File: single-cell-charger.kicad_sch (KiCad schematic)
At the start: 12 parts

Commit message: Lots of cleanup and updates; Waiting on PR approval for GPS filter
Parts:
- renumbered C35 to C43, C36 to C44, C37 to C45, D17 to D19, D18 to D20, U10 to U13, U11 to U14

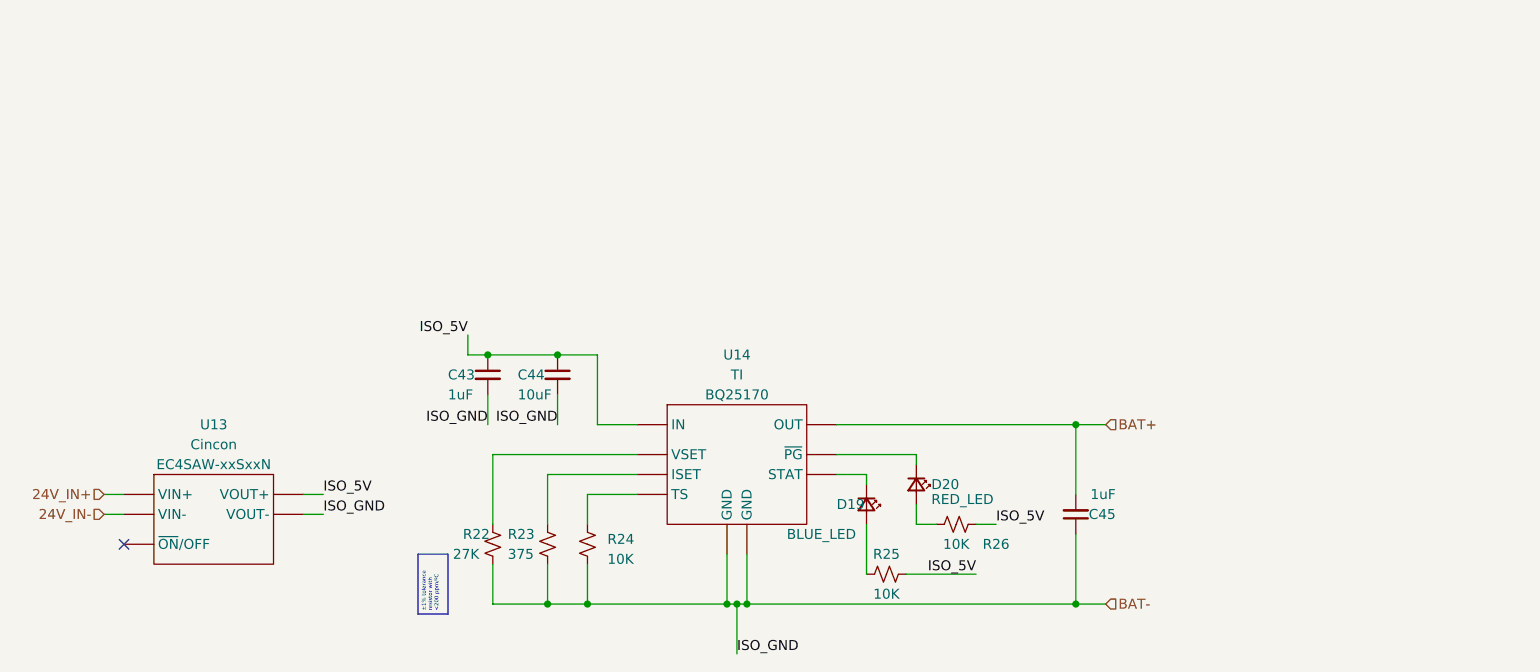
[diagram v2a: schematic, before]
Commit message: Added stat sense in REDs; kicad V8.01
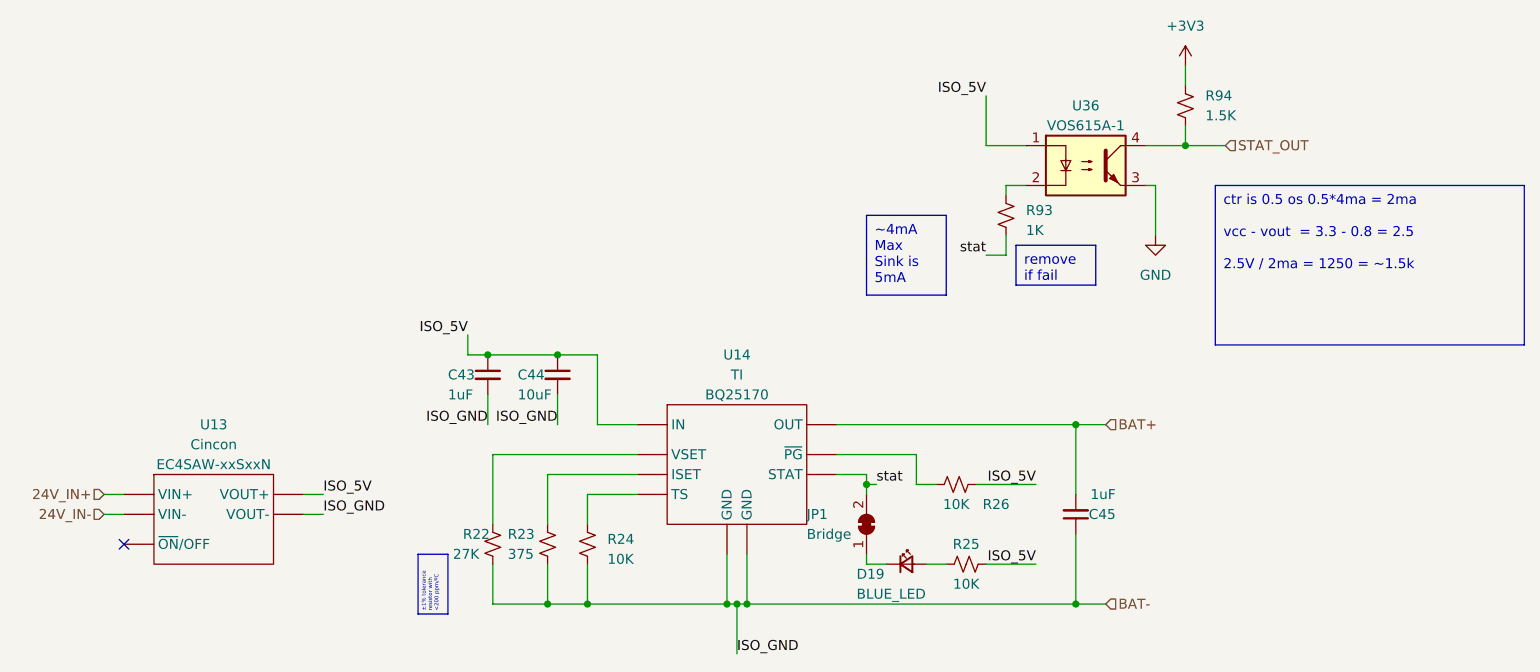
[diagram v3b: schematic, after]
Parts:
- removed D20: RED_LED, LED_SMD:LED_0603_1608Metric_Pad1.05x0.95mm_HandSolder, symbol Device:LED_Small
- added JP1: Bridge, symbol Jumper:SolderJumper_2_Bridged
- added R93: 1K, symbol Device:R_Small_US
- added R94: 1.5K, symbol Device:R_Small_US
- added U36: VOS615A-1, symbol Isolator:VO615A-1
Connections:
- net ISO_5V: now also U36.1
- net at R26.1: now also U14.6 (~{PG})
- net at D19.1 (K): now also JP1.1 (A); no longer U14.5 (STAT)
- new net: R93.1, U36.2
- new net +3V3: R94.1
- new net GND: U36.3
- new net STAT_OUT: R94.2, U36.4
- new net stat: JP1.2 (B), R93.2, U14.5 (STAT)
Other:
- moved on the sheet: D19, R25, R26

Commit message: 8.02 Update; Also changed VRMs and added some notes
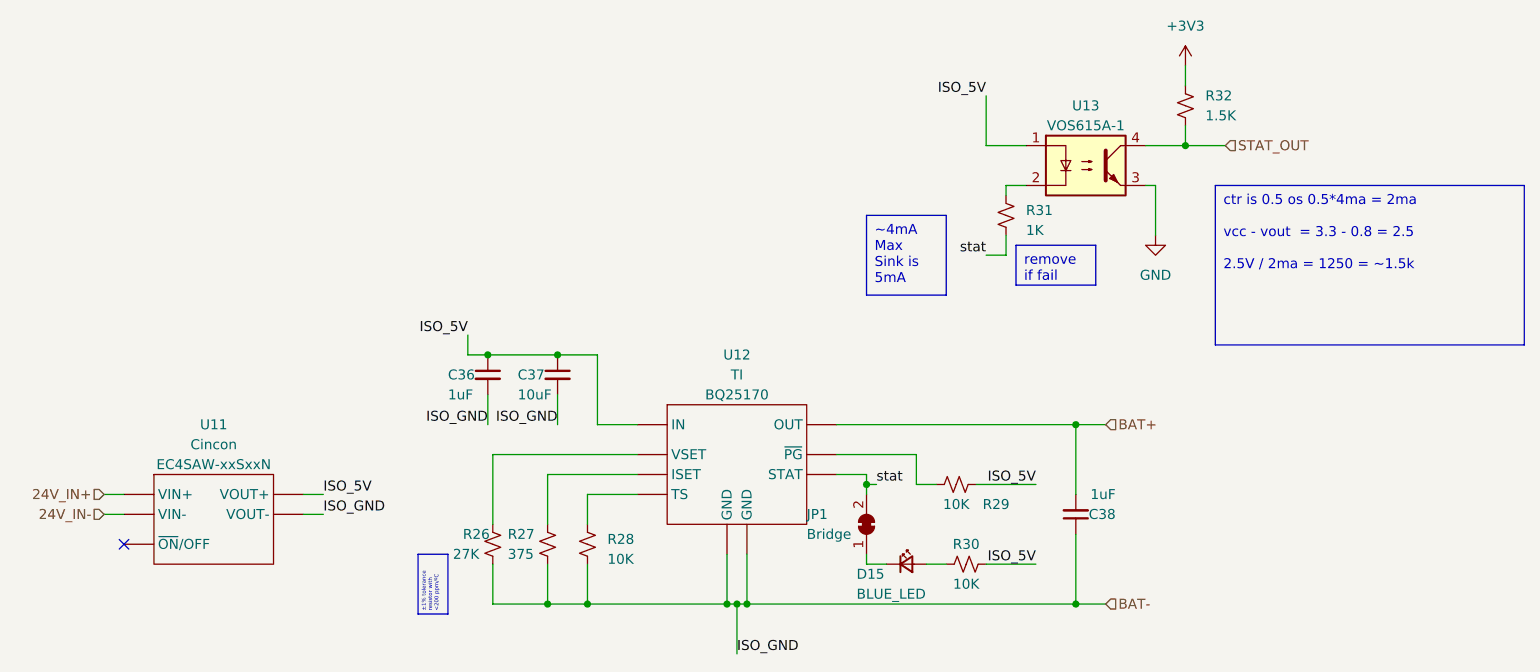
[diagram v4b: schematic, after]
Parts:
- renumbered C43 to C36, C44 to C37, C45 to C38, D19 to D15, R22 to R26, R23 to R27, R24 to R28, R26 to R29, R25 to R30, R93 to R31, R94 to R32, U13 to U11, U14 to U12, U36 to U13

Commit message: ECU essentially reviewable
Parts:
- renumbered D15 to D22, R26 to R30, R27 to R31, R28 to R32, R29 to R33, R30 to R34, R31 to R35, R32 to R36, U11 to U10, U12 to U11, U13 to U12

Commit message: addressed PR comments
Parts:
- renumbered D22 to D21
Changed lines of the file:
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@@
 		(dnp no)
 		(fields_autoplaced yes)
-		(property "Reference" "#PWR087"
+		(property "Reference" "#PWR088"
 			(at 205.74 46.99 0)
 			(effects
@@
 			(project "rocket2-ecu"
 				(path "/02606b2c-b376-4ffb-9781-f9cea3f70994/c8976b66-9d7c-47d1-8ab5-e6fd9c707361/218966e8-0599-4bad-8241-95ca09109d89"
-					(reference "#PWR087")
+					(reference "#PWR088")
 					(unit 1)
 				)
 				(path "/02606b2c-b376-4ffb-9781-f9cea3f70994/c8976b66-9d7c-47d1-8ab5-e6fd9c707361/1a39f8df-dcec-4a97-951c-60148a5067ca"
-					(reference "#PWR089")
+					(reference "#PWR090")
 					(unit 1)
 				)
 				(path "/02606b2c-b376-4ffb-9781-f9cea3f70994/c8976b66-9d7c-47d1-8ab5-e6fd9c707361/eb655268-f2ac-4ac0-945d-2ba286ede0a5"
-					(reference "#PWR091")
+					(reference "#PWR092")
 					(unit 1)
 				)
 				(path "/02606b2c-b376-4ffb-9781-f9cea3f70994/c8976b66-9d7c-47d1-8ab5-e6fd9c707361/b5f91759-085b-4a53-bede-6cb17536657b"
-					(reference "#PWR093")
+					(reference "#PWR094")
 					(unit 1)
 				)
 				(path "/02606b2c-b376-4ffb-9781-f9cea3f70994/c8976b66-9d7c-47d1-8ab5-e6fd9c707361/8ab1e7d4-e52f-422c-912d-30fd70001231"
-					(reference "#PWR095")
+					(reference "#PWR096")
 					(unit 1)
 				)
 				(path "/02606b2c-b376-4ffb-9781-f9cea3f70994/c8976b66-9d7c-47d1-8ab5-e6fd9c707361/5c1dbfcc-3925-4da2-a038-2c416606c068"
-					(reference "#PWR097")
+					(reference "#PWR098")
 					(unit 1)
 				)
@@
 		(dnp no)
 		(fields_autoplaced yes)
-		(property "Reference" "#PWR086"
+		(property "Reference" "#PWR087"
 			(at 201.93 71.12 0)
 			(effects
@@
 			(project "rocket2-ecu"
 				(path "/02606b2c-b376-4ffb-9781-f9cea3f70994/c8976b66-9d7c-47d1-8ab5-e6fd9c707361/218966e8-0599-4bad-8241-95ca09109d89"
-					(reference "#PWR086")
+					(reference "#PWR087")
 					(unit 1)
 				)
 				(path "/02606b2c-b376-4ffb-9781-f9cea3f70994/c8976b66-9d7c-47d1-8ab5-e6fd9c707361/1a39f8df-dcec-4a97-951c-60148a5067ca"
-					(reference "#PWR088")
+					(reference "#PWR089")
 					(unit 1)
 				)
 				(path "/02606b2c-b376-4ffb-9781-f9cea3f70994/c8976b66-9d7c-47d1-8ab5-e6fd9c707361/eb655268-f2ac-4ac0-945d-2ba286ede0a5"
-					(reference "#PWR090")
+					(reference "#PWR091")
 					(unit 1)
 				)
 				(path "/02606b2c-b376-4ffb-9781-f9cea3f70994/c8976b66-9d7c-47d1-8ab5-e6fd9c707361/b5f91759-085b-4a53-bede-6cb17536657b"
-					(reference "#PWR092")
+					(reference "#PWR093")
 					(unit 1)
 				)
 				(path "/02606b2c-b376-4ffb-9781-f9cea3f70994/c8976b66-9d7c-47d1-8ab5-e6fd9c707361/8ab1e7d4-e52f-422c-912d-30fd70001231"
-					(reference "#PWR094")
+					(reference "#PWR095")
 					(unit 1)
 				)
 				(path "/02606b2c-b376-4ffb-9781-f9cea3f70994/c8976b66-9d7c-47d1-8ab5-e6fd9c707361/5c1dbfcc-3925-4da2-a038-2c416606c068"
-					(reference "#PWR096")
+					(reference "#PWR097")
 					(unit 1)
 				)
@@
 		(on_board yes)
 		(dnp no)
-		(property "Reference" "D22"
+		(property "Reference" "D21"
 			(at 163.83 107.95 0)
 			(effects
@@
 			(project "rocket2-ecu"
 				(path "/02606b2c-b376-4ffb-9781-f9cea3f70994/c8976b66-9d7c-47d1-8ab5-e6fd9c707361/5c1dbfcc-3925-4da2-a038-2c416606c068"
-					(reference "D22")
+					(reference "D21")
 					(unit 1)
 				)
 				(path "/02606b2c-b376-4ffb-9781-f9cea3f70994/c8976b66-9d7c-47d1-8ab5-e6fd9c707361/8ab1e7d4-e52f-422c-912d-30fd70001231"
-					(reference "D21")
+					(reference "D20")
 					(unit 1)
 				)
 				(path "/02606b2c-b376-4ffb-9781-f9cea3f70994/c8976b66-9d7c-47d1-8ab5-e6fd9c707361/b5f91759-085b-4a53-bede-6cb17536657b"
-					(reference "D20")
+					(reference "D19")
 					(unit 1)
 				)
 				(path "/02606b2c-b376-4ffb-9781-f9cea3f70994/c8976b66-9d7c-47d1-8ab5-e6fd9c707361/eb655268-f2ac-4ac0-945d-2ba286ede0a5"
-					(reference "D19")
+					(reference "D18")
 					(unit 1)
 				)
 				(path "/02606b2c-b376-4ffb-9781-f9cea3f70994/c8976b66-9d7c-47d1-8ab5-e6fd9c707361/1a39f8df-dcec-4a97-951c-60148a5067ca"
-					(reference "D18")
+					(reference "D17")
 					(unit 1)
 				)
 				(path "/02606b2c-b376-4ffb-9781-f9cea3f70994/c8976b66-9d7c-47d1-8ab5-e6fd9c707361/218966e8-0599-4bad-8241-95ca09109d89"
-					(reference "D17")
-					(unit 1)
-				)
+					(reference "D16")
+					(unit 1)
+				)

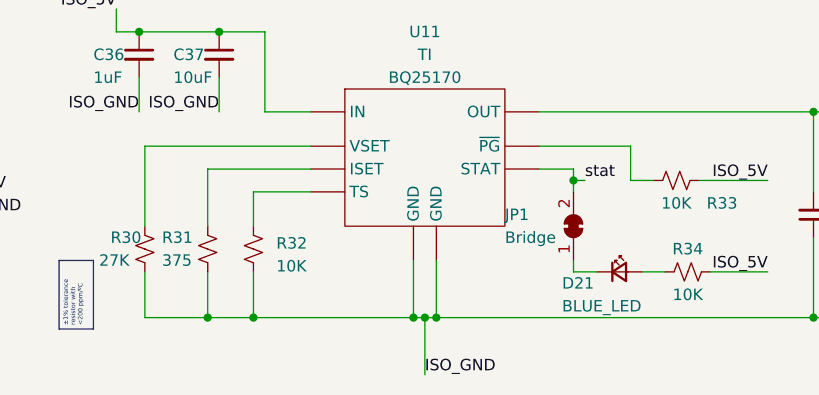
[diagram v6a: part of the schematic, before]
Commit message: Assigned almost all footprints
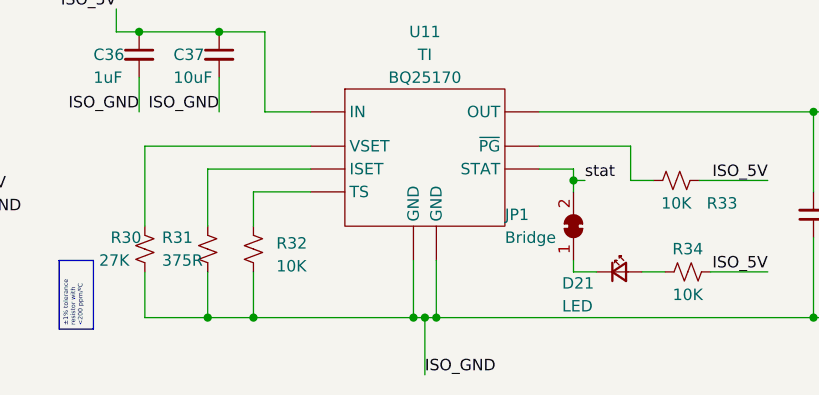
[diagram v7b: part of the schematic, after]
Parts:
- C36, C37, C38: footprint Capacitor_SMD:C_0603_1608Metric_Pad1.08x0.95mm_HandSolder -> Capacitor_SMD:C_0603_1608Metric
- D21: value BLUE_LED -> LED
- JP1: footprint (none) -> Jumper:SolderJumper-2_P1.3mm_Open_RoundedPad1.0x1.5mm
- R30: footprint Resistor_SMD:R_0603_1608Metric_Pad0.98x0.95mm_HandSolder -> Resistor_SMD:R_0603_1608Metric
- R31: value 375 -> 375R; footprint Resistor_SMD:R_0603_1608Metric_Pad0.98x0.95mm_HandSolder -> Resistor_SMD:R_0402_1005Metric; Part # Generic 0603 375ohm 0.1% Resistor -> Generic 0402 375ohm 0.1% Resistor
- R32, R33, R34: footprint Resistor_SMD:R_0603_1608Metric_Pad0.98x0.95mm_HandSolder -> Resistor_SMD:R_0402_1005Metric; Part # Generic 0603 10K 1% Resistor -> Generic 10K 1% 0402 Resistor
- R35: footprint (none) -> Resistor_SMD:R_0402_1005Metric; Part # (none) -> Generic 1K 1% 0402 Resistor
- R36: footprint (none) -> Resistor_SMD:R_0402_1005Metric; Part # (none) -> Generic 0402 1.5K 0.1% Resistor
- U10: footprint UCIRP-KiCAD-Lib:EC4SAW-xxSxxN -> 0UCIRP-KiCAD-Lib:EC4SAW-xxSxxN
- U12: footprint (none) -> Package_SO:SOP-4_4.4x2.6mm_P1.27mm
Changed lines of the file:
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@@
 			)
 		)
-		(property "Footprint" ""
+		(property "Footprint" "Resistor_SMD:R_0402_1005Metric"
 			(at 182.88 62.23 0)
 			(effects
@@
 		)
 		(property "Description" ""
+			(at 182.88 62.23 0)
+			(effects
+				(font
+					(size 1.27 1.27)
+				)
+				(hide yes)
+			)
+		)
+		(property "Part #" "Generic 1K 1% 0402 Resistor"
 			(at 182.88 62.23 0)
 			(effects
@@
 			)
 		)
-		(property "Footprint" "UCIRP-KiCAD-Lib:EC4SAW-xxSxxN"
+		(property "Footprint" "0UCIRP-KiCAD-Lib:EC4SAW-xxSxxN"
 			(at 81.915 100.33 0)
 			(effects
@@
 			)
 		)
-		(property "Footprint" "Resistor_SMD:R_0603_1608Metric_Pad0.98x0.95mm_HandSolder"
+		(property "Footprint" "Resistor_SMD:R_0402_1005Metric"
 			(at 176.53 96.52 0)
 			(effects
@@
 			)
 		)
-		(property "Part #" "Generic 0603 10K 1% Resistor"
+		(property "Part #" "Generic 10K 1% 0402 Resistor"
 			(at 176.53 96.52 0)
 			(effects
@@
 			)
 		)
-		(property "Footprint" "Capacitor_SMD:C_0603_1608Metric_Pad1.08x0.95mm_HandSolder"
+		(property "Footprint" "Capacitor_SMD:C_0603_1608Metric"
 			(at 116.84 82.55 0)
 			(effects
@@
 			)
 		)
-		(property "Footprint" "Capacitor_SMD:C_0603_1608Metric_Pad1.08x0.95mm_HandSolder"
+		(property "Footprint" "Capacitor_SMD:C_0603_1608Metric"
 			(at 191.77 100.33 0)
 			(effects
@@
 			)
 		)
-		(property "Footprint" ""
+		(property "Footprint" "Resistor_SMD:R_0402_1005Metric"
 			(at 205.74 48.26 0)
 			(effects
@@
 		)
 		(property "Description" ""
+			(at 205.74 48.26 0)
+			(effects
+				(font
+					(size 1.27 1.27)
+				)
+				(hide yes)
+			)
+		)
+		(property "Part #" "Generic 0402 1.5K 0.1% Resistor"
 			(at 205.74 48.26 0)
 			(effects
@@
 			)
 		)
-		(property "Footprint" ""
+		(property "Footprint" "Jumper:SolderJumper-2_P1.3mm_Open_RoundedPad1.0x1.5mm"
 			(at 165.1 101.6 0)
 			(effects
@@
 			)
 		)
-		(property "Footprint" ""
+		(property "Footprint" "Package_SO:SOP-4_4.4x2.6mm_P1.27mm"
 			(at 193.04 55.88 0)
 			(effects
@@
 			)
 		)
-		(property "Footprint" "Resistor_SMD:R_0603_1608Metric_Pad0.98x0.95mm_HandSolder"
+		(property "Footprint" "Resistor_SMD:R_0402_1005Metric"
 			(at 177.8 106.68 0)
 			(effects
@@
 			)
 		)
-		(property "Part #" "Generic 0603 10K 1% Resistor"
+		(property "Part #" "Generic 10K 1% 0402 Resistor"
 			(at 177.8 106.68 0)
 			(effects
@@
 			)
 		)
-		(property "Footprint" "Resistor_SMD:R_0603_1608Metric_Pad0.98x0.95mm_HandSolder"
+		(property "Footprint" "Resistor_SMD:R_0603_1608Metric"
 			(at 117.475 104.14 0)
 			(effects
@@
 			)
 		)
-		(property "Footprint" "Resistor_SMD:R_0603_1608Metric_Pad0.98x0.95mm_HandSolder"
+		(property "Footprint" "Resistor_SMD:R_0402_1005Metric"
 			(at 129.54 104.14 0)
 			(effects
@@
 			)
 		)
-		(property "Part #" "Generic 0603 10K 1% Resistor"
+		(property "Part #" "Generic 10K 1% 0402 Resistor"
 			(at 129.54 104.14 0)
 			(effects
@@
 			)
 		)
-		(property "Value" "375"
+		(property "Value" "375R"
 			(at 119.38 105.41 0)
 			(effects
@@
 			)
 		)
-		(property "Footprint" "Resistor_SMD:R_0603_1608Metric_Pad0.98x0.95mm_HandSolder"
+		(property "Footprint" "Resistor_SMD:R_0402_1005Metric"
 			(at 124.46 104.14 0)
 			(effects
@@
 			)
 		)
-		(property "Part #" "Generic 0603 375ohm 0.1% Resistor"
+		(property "Part #" "Generic 0402 375ohm 0.1% Resistor"
 			(at 124.46 104.14 0)
 			(effects
@@
 			)
 		)
-		(property "Footprint" "Capacitor_SMD:C_0603_1608Metric_Pad1.08x0.95mm_HandSolder"
+		(property "Footprint" "Capacitor_SMD:C_0603_1608Metric"
 			(at 125.73 82.55 0)
 			(effects
@@
 			)
 		)
-		(property "Value" "BLUE_LED"
+		(property "Value" "LED"
 			(at 163.83 110.49 0)
 			(effects

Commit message: new BOM
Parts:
- C36, C38: Part # Generic 0603 1uF 6.3V X7R MLCC -> Generic CAP CER 1UF 50V X7R 0603
- C37: Part # Generic 0603 10uF 6.3V X7R MLCC -> Generic CAP CER 10UF 50V X7R 0603
- R30: Manufacturer Bourns -> Bourns Inc.
- R31: value 375R -> 375; Part # Generic 0402 375ohm 0.1% Resistor -> Generic RES SMD 375 OHM 0.1% 1/16W 0402
- R32, R33, R34: Part # Generic 10K 1% 0402 Resistor -> Generic RES SMD 10K OHM 1% 1/4W 0402
- R35: Manufacturer (none) -> Generic; Part # Generic 1K 1% 0402 Resistor -> Generic RES SMD 1K OHM 1% 1/16W 0402
- R36: Manufacturer (none) -> Generic; Part # Generic 0402 1.5K 0.1% Resistor -> Generic RES SMD 1.5K OHM 0.1% 1/16W 0402
- U11: Manufacturer TI -> Texas Instruments
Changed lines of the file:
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@@
 			)
 		)
-		(property "Part #" "Generic 1K 1% 0402 Resistor"
+		(property "Part #" "Generic RES SMD 1K OHM 1% 1/16W 0402"
+			(at 182.88 62.23 0)
+			(effects
+				(font
+					(size 1.27 1.27)
+				)
+				(hide yes)
+			)
+		)
+		(property "Manufacturer" "Generic"
 			(at 182.88 62.23 0)
 			(effects
@@
 			)
 		)
-		(property "Part #" "Generic 10K 1% 0402 Resistor"
+		(property "Part #" "Generic RES SMD 10K OHM 1% 1/4W 0402"
 			(at 176.53 96.52 0)
 			(effects
@@
 			)
 		)
-		(property "Part #" "Generic 0603 1uF 6.3V X7R MLCC"
+		(property "Part #" "Generic CAP CER 1UF 50V X7R 0603"
 			(at 116.84 82.55 0)
 			(effects
@@
 			)
 		)
-		(property "Part #" "Generic 0603 1uF 6.3V X7R MLCC"
+		(property "Part #" "Generic CAP CER 1UF 50V X7R 0603"
 			(at 191.77 100.33 0)
 			(effects
@@
 			)
 		)
-		(property "Part #" "Generic 0402 1.5K 0.1% Resistor"
+		(property "Part #" "Generic RES SMD 1.5K OHM 0.1% 1/16W 0402"
+			(at 205.74 48.26 0)
+			(effects
+				(font
+					(size 1.27 1.27)
+				)
+				(hide yes)
+			)
+		)
+		(property "Manufacturer" "Generic"
 			(at 205.74 48.26 0)
 			(effects
@@
 			)
 		)
-		(property "Part #" "Generic 10K 1% 0402 Resistor"
+		(property "Part #" "Generic RES SMD 10K OHM 1% 1/4W 0402"
 			(at 177.8 106.68 0)
 			(effects
@@
 			)
 		)
-		(property "Manufacturer" "Bourns"
+		(property "Manufacturer" "Bourns Inc."
 			(at 117.475 104.14 0)
 			(effects
@@
 			)
 		)
-		(property "Part #" "Generic 10K 1% 0402 Resistor"
+		(property "Part #" "Generic RES SMD 10K OHM 1% 1/4W 0402"
 			(at 129.54 104.14 0)
 			(effects
@@
 			)
 		)
-		(property "Value" "375R"
+		(property "Value" "375"
 			(at 119.38 105.41 0)
 			(effects
@@
 			)
 		)
-		(property "Part #" "Generic 0402 375ohm 0.1% Resistor"
+		(property "Part #" "Generic RES SMD 375 OHM 0.1% 1/16W 0402"
 			(at 124.46 104.14 0)
 			(effects
@@
 			)
 		)
-		(property "Manufacturer" "TI"
+		(property "Manufacturer" "Texas Instruments"
 			(at 148.59 82.55 0)
 			(effects
@@
 			)
 		)
-		(property "Part #" "Generic 0603 10uF 6.3V X7R MLCC"
+		(property "Part #" "Generic CAP CER 10UF 50V X7R 0603"
 			(at 125.73 82.55 0)
 			(effects
